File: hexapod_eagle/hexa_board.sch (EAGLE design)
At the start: 52 parts

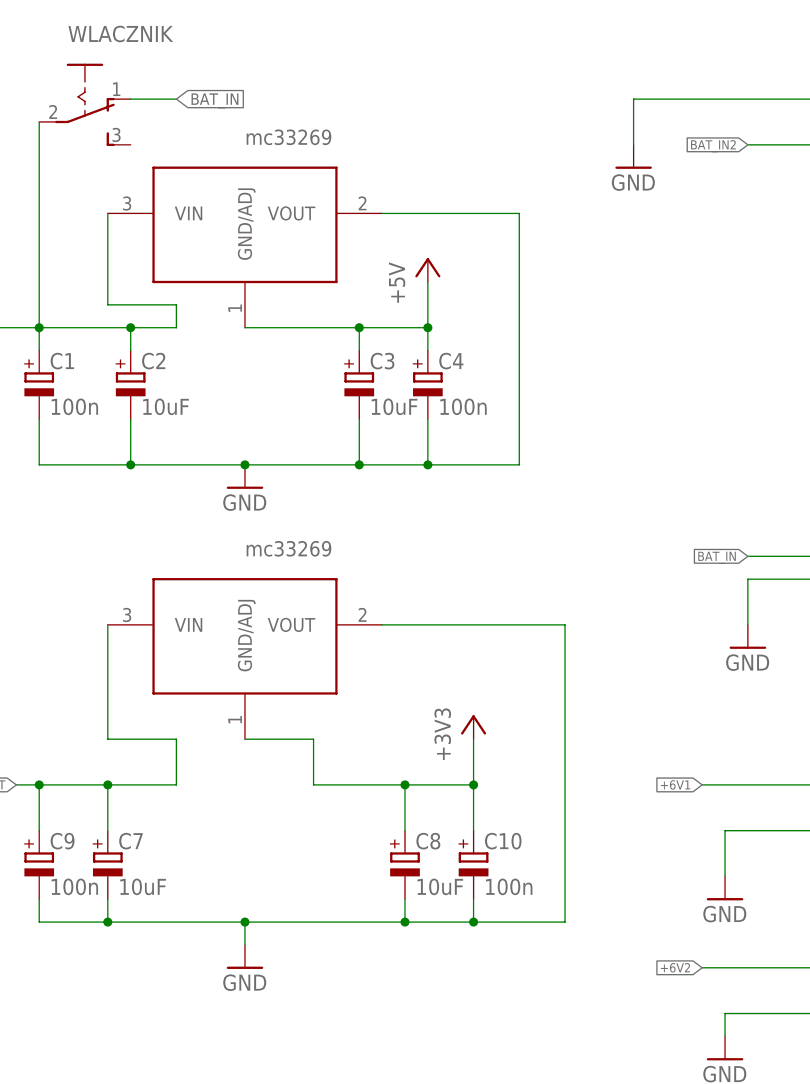
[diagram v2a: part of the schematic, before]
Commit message: Update board project
-fix voltage regulator output
-added tantalum capacitors (B size)instead cpol
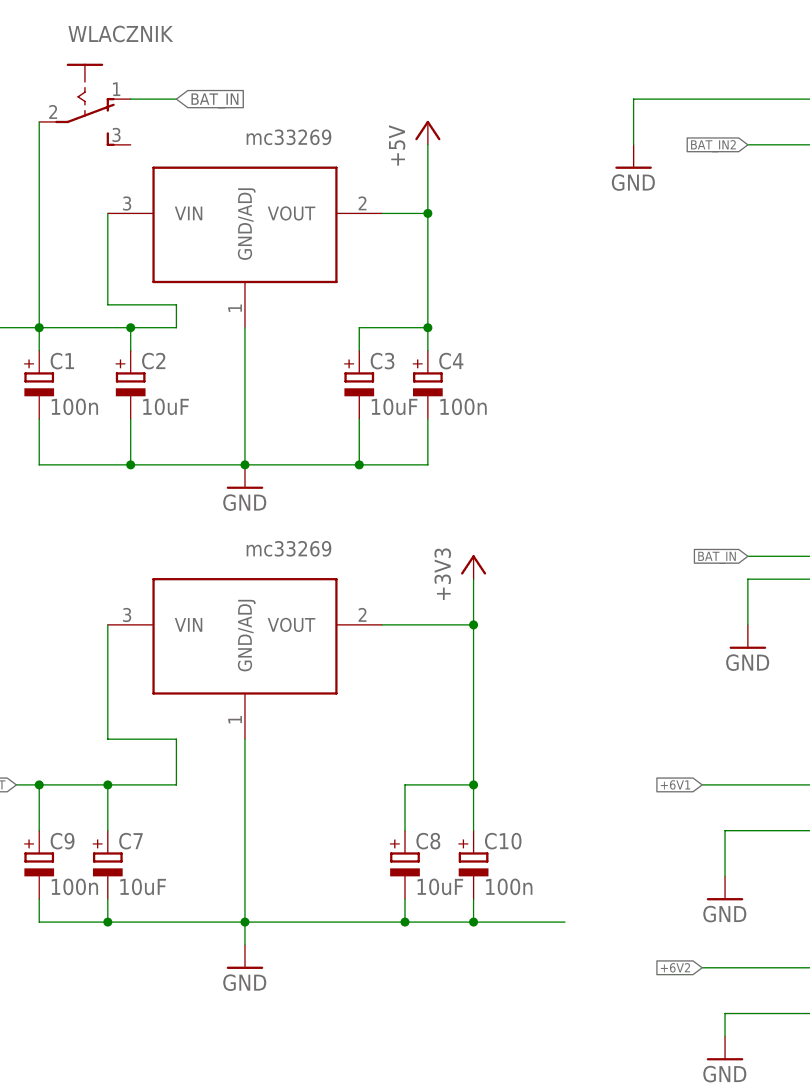
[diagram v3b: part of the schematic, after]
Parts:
- C2, C3, C7, C8: device rcl:CPOL-EUSMCA -> rcl:CPOL-EUSMCB
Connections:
- net +3V3: now also 3V.VOUT; no longer 3V.GND/ADJ
- net +5V: now also 5V.VOUT; no longer 5V.GND/ADJ
- net GND: now also 3V.GND/ADJ, 5V.GND/ADJ; no longer 3V.VOUT, 5V.VOUT
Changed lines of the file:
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@@
 <part name="+3V4" library="supply1" deviceset="+3V3" device=""/>
 <part name="MPU6050" library="pinhead" deviceset="PINHD-1X5" device=""/>
-<part name="C7" library="rcl" deviceset="CPOL-EU" device="SMCA" value="10uF"/>
-<part name="C8" library="rcl" deviceset="CPOL-EU" device="SMCA" value="10uF"/>
+<part name="C7" library="rcl" deviceset="CPOL-EU" device="SMCB" value="10uF"/>
+<part name="C8" library="rcl" deviceset="CPOL-EU" device="SMCB" value="10uF"/>
 <part name="+3V5" library="supply1" deviceset="+3V3" device=""/>
 <part name="GND11" library="supply1" deviceset="GND" device=""/>
@@
 <part name="GND1" library="supply1" deviceset="GND" device=""/>
 <part name="C1" library="rcl" deviceset="CPOL-EU" device="SMCA" value="100n"/>
-<part name="C2" library="rcl" deviceset="CPOL-EU" device="SMCA" value="10uF"/>
-<part name="C3" library="rcl" deviceset="CPOL-EU" device="SMCA" value="10uF"/>
+<part name="C2" library="rcl" deviceset="CPOL-EU" device="SMCB" value="10uF"/>
+<part name="C3" library="rcl" deviceset="CPOL-EU" device="SMCB" value="10uF"/>
 <part name="C4" library="rcl" deviceset="CPOL-EU" device="SMCA" value="100n"/>
 <part name="P+1" library="supply1" deviceset="+5V" device=""/>
@@
 <instance part="C7" gate="G$1" x="10.16" y="210.82"/>
 <instance part="C8" gate="G$1" x="43.18" y="210.82"/>
-<instance part="+3V5" gate="G$1" x="50.8" y="226.06"/>
+<instance part="+3V5" gate="G$1" x="50.8" y="243.84"/>
 <instance part="GND11" gate="1" x="25.4" y="198.12"/>
 <instance part="GND12" gate="1" x="78.74" y="187.96"/>
@@
 <instance part="C3" gate="G$1" x="38.1" y="264.16"/>
 <instance part="C4" gate="G$1" x="45.72" y="264.16"/>
-<instance part="P+1" gate="1" x="45.72" y="276.86"/>
+<instance part="P+1" gate="1" x="45.72" y="292.1"/>
 <instance part="WIFI" gate="G$1" x="154.94" y="139.7"/>
 <instance part="GND2" gate="1" x="185.42" y="129.54"/>
@@
 </segment>
 <segment>
-<wire x1="33.02" y1="218.44" x2="43.18" y2="218.44" width="0.1524" layer="91"/>
 <pinref part="C8" gate="G$1" pin="+"/>
 <wire x1="43.18" y1="218.44" x2="43.18" y2="213.36" width="0.1524" layer="91"/>
 <wire x1="43.18" y1="218.44" x2="50.8" y2="218.44" width="0.1524" layer="91"/>
-<junction x="43.18" y="218.44"/>
 <pinref part="+3V5" gate="G$1" pin="+3V3"/>
-<wire x1="50.8" y1="218.44" x2="50.8" y2="223.52" width="0.1524" layer="91"/>
+<wire x1="50.8" y1="218.44" x2="50.8" y2="236.22" width="0.1524" layer="91"/>
 <pinref part="C10" gate="G$1" pin="+"/>
+<wire x1="50.8" y1="236.22" x2="50.8" y2="241.3" width="0.1524" layer="91"/>
 <wire x1="50.8" y1="218.44" x2="50.8" y2="213.36" width="0.1524" layer="91"/>
 <junction x="50.8" y="218.44"/>
-<pinref part="3V" gate="G$1" pin="GND/ADJ"/>
-<wire x1="25.4" y1="223.52" x2="33.02" y2="223.52" width="0.1524" layer="91"/>
-<wire x1="33.02" y1="223.52" x2="33.02" y2="218.44" width="0.1524" layer="91"/>
+<pinref part="3V" gate="G$1" pin="VOUT"/>
+<wire x1="40.64" y1="236.22" x2="50.8" y2="236.22" width="0.1524" layer="91"/>
+<junction x="50.8" y="236.22"/>
 </segment>
 <segment>
@@
 <wire x1="50.8" y1="203.2" x2="50.8" y2="205.74" width="0.1524" layer="91"/>
 <junction x="43.18" y="203.2"/>
-<pinref part="3V" gate="G$1" pin="VOUT"/>
-<wire x1="40.64" y1="236.22" x2="60.96" y2="236.22" width="0.1524" layer="91"/>
-<wire x1="60.96" y1="236.22" x2="60.96" y2="203.2" width="0.1524" layer="91"/>
 <wire x1="60.96" y1="203.2" x2="50.8" y2="203.2" width="0.1524" layer="91"/>
 <junction x="50.8" y="203.2"/>
+<pinref part="3V" gate="G$1" pin="GND/ADJ"/>
+<wire x1="25.4" y1="223.52" x2="25.4" y2="203.2" width="0.1524" layer="91"/>
 </segment>
 <segment>
@@
 <wire x1="45.72" y1="254" x2="45.72" y2="259.08" width="0.1524" layer="91"/>
 <junction x="38.1" y="254"/>
-<wire x1="45.72" y1="254" x2="55.88" y2="254" width="0.1524" layer="91"/>
-<junction x="45.72" y="254"/>
-<pinref part="5V" gate="G$1" pin="VOUT"/>
-<wire x1="40.64" y1="281.94" x2="55.88" y2="281.94" width="0.1524" layer="91"/>
-<wire x1="55.88" y1="254" x2="55.88" y2="281.94" width="0.1524" layer="91"/>
+<pinref part="5V" gate="G$1" pin="GND/ADJ"/>
+<wire x1="25.4" y1="269.24" x2="25.4" y2="254" width="0.1524" layer="91"/>
 </segment>
 <segment>
@@
 <wire x1="38.1" y1="269.24" x2="45.72" y2="269.24" width="0.1524" layer="91"/>
 <wire x1="45.72" y1="269.24" x2="45.72" y2="266.7" width="0.1524" layer="91"/>
-<junction x="38.1" y="269.24"/>
-<wire x1="45.72" y1="269.24" x2="45.72" y2="274.32" width="0.1524" layer="91"/>
+<wire x1="45.72" y1="269.24" x2="45.72" y2="281.94" width="0.1524" layer="91"/>
 <junction x="45.72" y="269.24"/>
 <pinref part="P+1" gate="1" pin="+5V"/>
-<pinref part="5V" gate="G$1" pin="GND/ADJ"/>
-<wire x1="38.1" y1="269.24" x2="25.4" y2="269.24" width="0.1524" layer="91"/>
-</segment>
-<segment>
+<pinref part="5V" gate="G$1" pin="VOUT"/>
+<wire x1="45.72" y1="281.94" x2="45.72" y2="289.56" width="0.1524" layer="91"/>
+<wire x1="40.64" y1="281.94" x2="45.72" y2="281.94" width="0.1524" layer="91"/>
+<junction x="45.72" y="281.94"/>
+</segment>
+<segment>

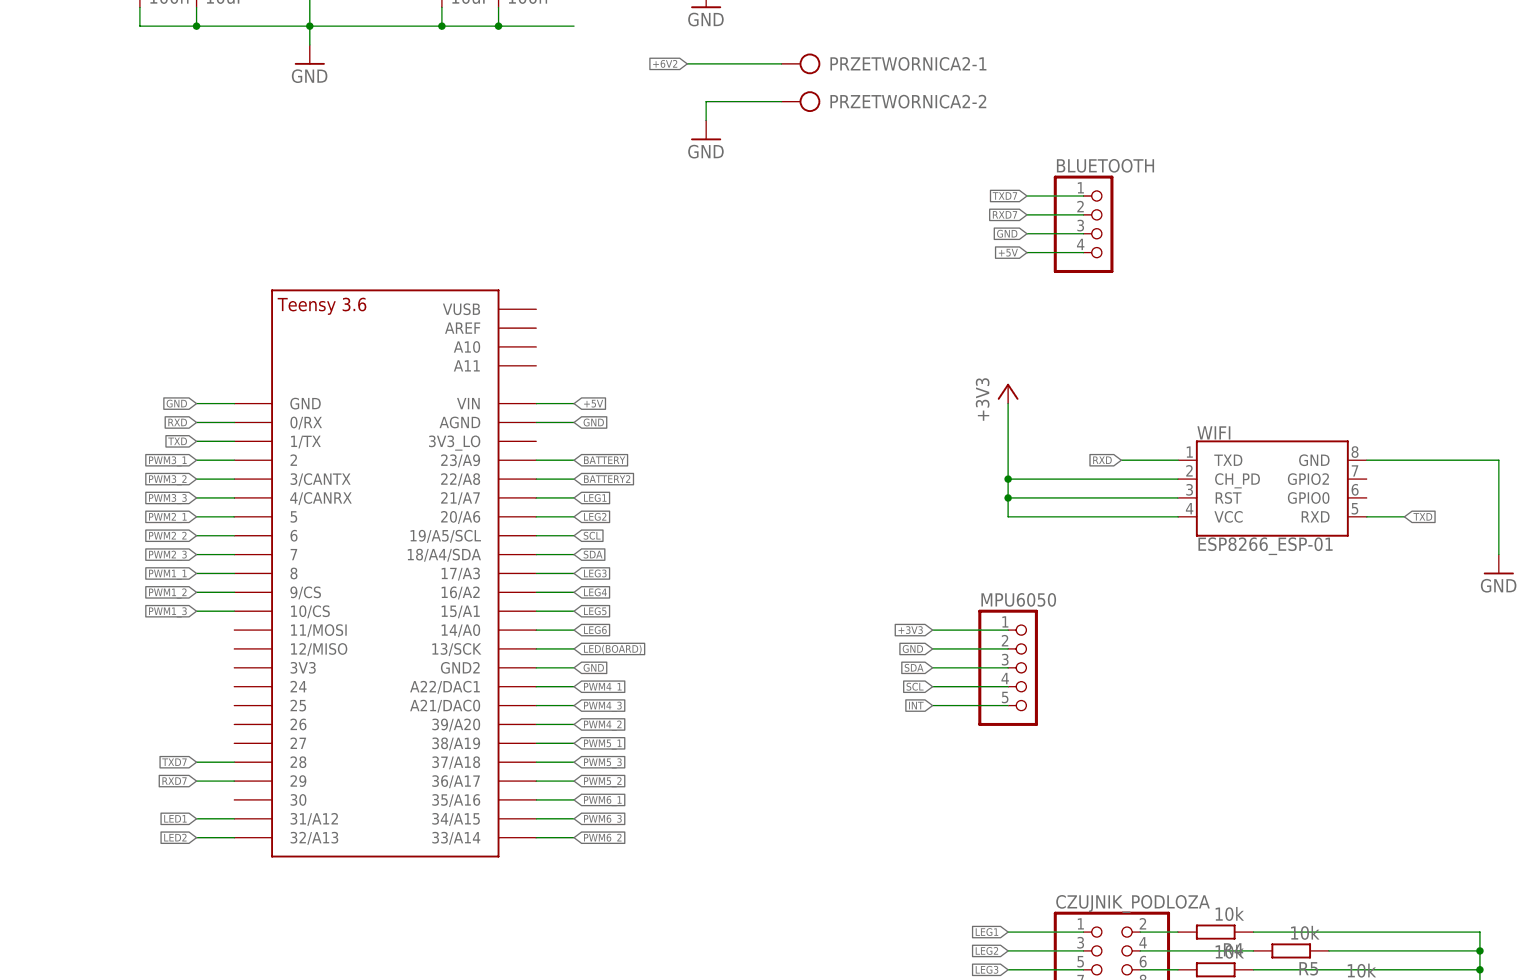
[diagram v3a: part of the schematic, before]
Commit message: Update eagle board
-added sharp sensor
-some minor changes
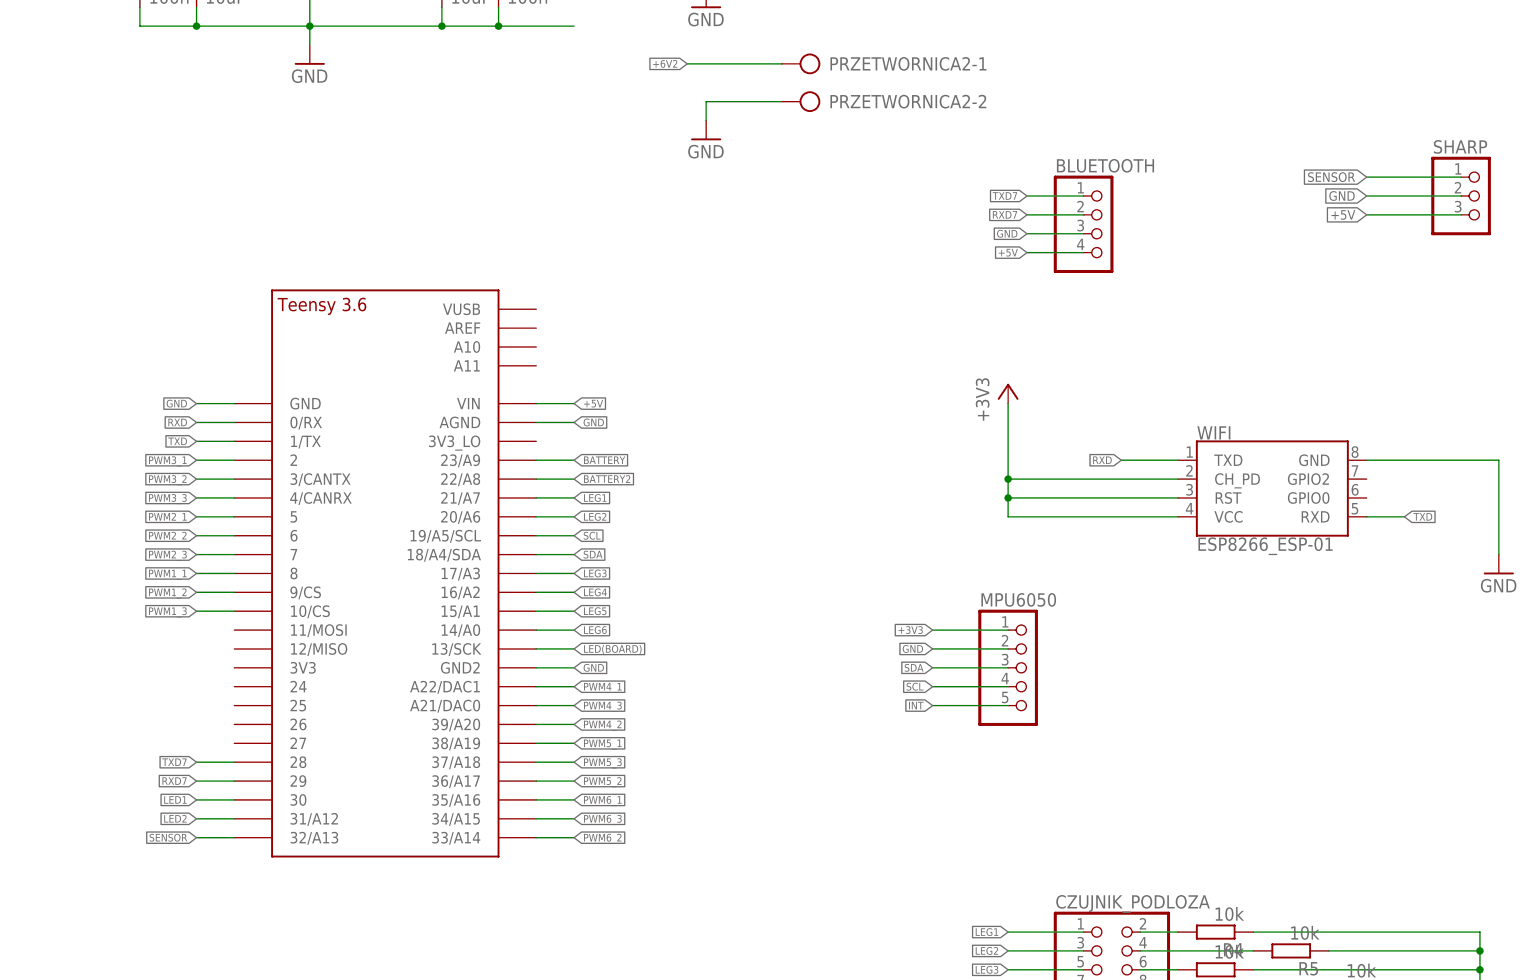
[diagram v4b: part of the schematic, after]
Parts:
- added SHARP: (no value), pinhead:PINHD-1X3
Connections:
- new net SENSOR: SHARP.1, TEENSY41.32/A13
- net +5V: now also SHARP.3
- net GND: now also SHARP.2
- net LED1: now also TEENSY41.30; no longer TEENSY41.31/A12
- net LED2: now also TEENSY41.31/A12; no longer TEENSY41.32/A13
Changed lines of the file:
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@@
 <part name="GND10" library="supply1" deviceset="GND" device=""/>
 <part name="GND14" library="supply1" deviceset="GND" device=""/>
+<part name="SHARP" library="pinhead" deviceset="PINHD-1X3" device=""/>
 </parts>
 <sheets>
@@
 <instance part="GND10" gate="1" x="124.46" y="12.7"/>
 <instance part="GND14" gate="1" x="134.62" y="12.7"/>
+<instance part="SHARP" gate="A" x="182.88" y="180.34"/>
 </instances>
 <busses>
@@
 <wire x1="134.62" y1="20.32" x2="134.62" y2="15.24" width="0.1524" layer="91"/>
 </segment>
+<segment>
+<pinref part="SHARP" gate="A" pin="2"/>
+<wire x1="180.34" y1="180.34" x2="167.64" y2="180.34" width="0.1524" layer="91"/>
+<label x="167.64" y="180.34" size="1.27" layer="95" rot="R180" xref="yes"/>
+</segment>
 </net>
 <net name="INT" class="0">
@@
 <label x="121.92" y="172.72" size="1.016" layer="95" rot="R180" xref="yes"/>
 </segment>
+<segment>
+<pinref part="SHARP" gate="A" pin="3"/>
+<wire x1="180.34" y1="177.8" x2="167.64" y2="177.8" width="0.1524" layer="91"/>
+<label x="167.64" y="177.8" size="1.27" layer="95" rot="R180" xref="yes"/>
+</segment>
 </net>
 <net name="RXD" class="0">
@@
 </segment>
 <segment>
+<pinref part="TEENSY41" gate="G$1" pin="30"/>
+<wire x1="15.24" y1="99.06" x2="10.16" y2="99.06" width="0.1524" layer="91"/>
+<label x="10.16" y="99.06" size="1.016" layer="95" rot="R180" xref="yes"/>
+</segment>
+</net>
+<net name="LED2" class="0">
+<segment>
+<pinref part="LED_COM2" gate="G$1" pin="A"/>
+<wire x1="134.62" y1="40.64" x2="134.62" y2="45.72" width="0.1524" layer="91"/>
+<label x="134.62" y="45.72" size="1.778" layer="95" rot="R90" xref="yes"/>
+</segment>
+<segment>
 <pinref part="TEENSY41" gate="G$1" pin="31/A12"/>
 <wire x1="15.24" y1="96.52" x2="10.16" y2="96.52" width="0.1524" layer="91"/>
@@
 </segment>
 </net>
-<net name="LED2" class="0">
-<segment>
-<pinref part="LED_COM2" gate="G$1" pin="A"/>
-<wire x1="134.62" y1="40.64" x2="134.62" y2="45.72" width="0.1524" layer="91"/>
-<label x="134.62" y="45.72" size="1.778" layer="95" rot="R90" xref="yes"/>
-</segment>
+<net name="SENSOR" class="0">
 <segment>
 <pinref part="TEENSY41" gate="G$1" pin="32/A13"/>
@@
 <label x="10.16" y="93.98" size="1.016" layer="95" rot="R180" xref="yes"/>
 </segment>
-</net>
+<segment>
+<pinref part="SHARP" gate="A" pin="1"/>
+<wire x1="180.34" y1="182.88" x2="167.64" y2="182.88" width="0.1524" layer="91"/>
+<label x="167.64" y="182.88" size="1.27" layer="95" rot="R180" xref="yes"/>
+</segment>
+</net>
